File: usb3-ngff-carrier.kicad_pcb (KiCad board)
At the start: 4 copper layers, 90 x 40 mm, 70 parts, among them J1 KUSBX-BS1N9-1-BL30, J2 2199119-3, J3 Jack-DC, J5 Conn_01x03_Male, J6 SIM2070-6-1-30-00-A, J8 SIM2070-6-1-30-00-A, SW1 KMR221GLFS, U1 AP62301WU7

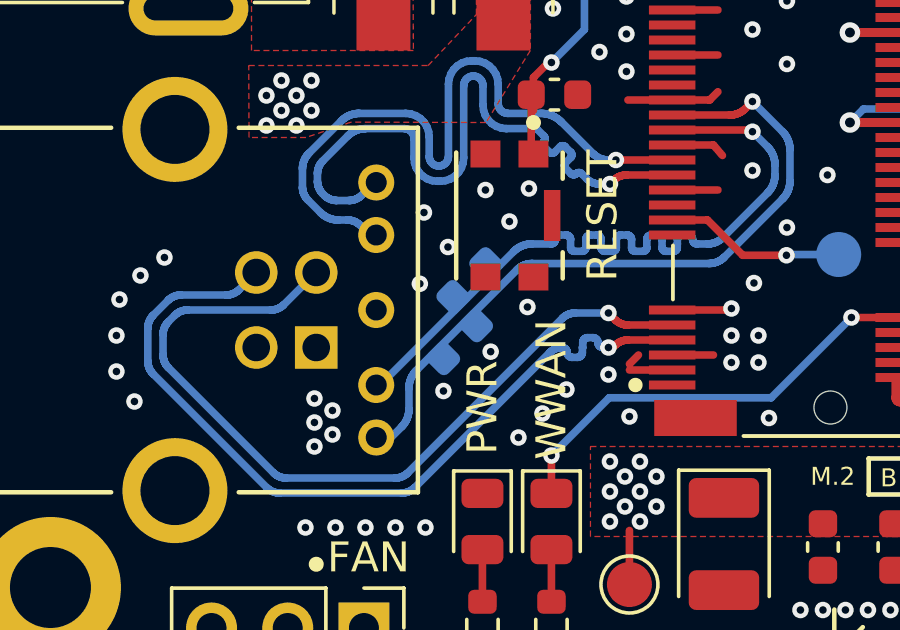
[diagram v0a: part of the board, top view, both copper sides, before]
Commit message: fix: reduces optional USB Caps pads to 0402 and exposes a piece of their track
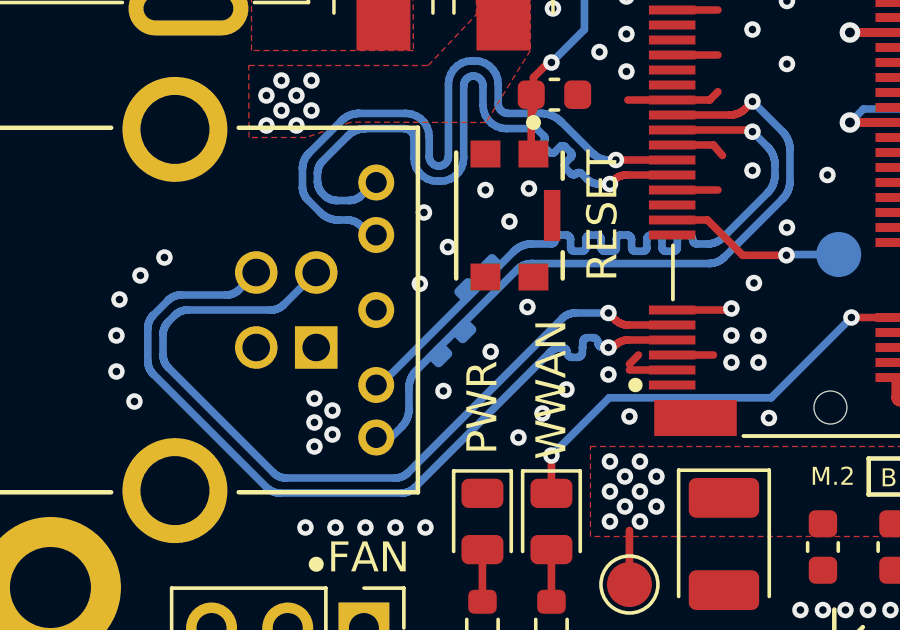
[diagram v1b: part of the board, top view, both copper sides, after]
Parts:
- C24, C25: value 33pF -> 0.22uF; footprint Capacitor_SMD:C_0603_1608Metric -> Capacitor_SMD:C_0402_1005Metric_Pad0.74x0.62mm_HandSolder
- moved C25 0.31 mm to (87.3, 71.5)
- moved C24 0.27 mm to (86.4, 73.7)
